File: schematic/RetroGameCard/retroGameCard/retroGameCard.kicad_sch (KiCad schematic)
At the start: 1 part, among them IC1 STM32C562KET6

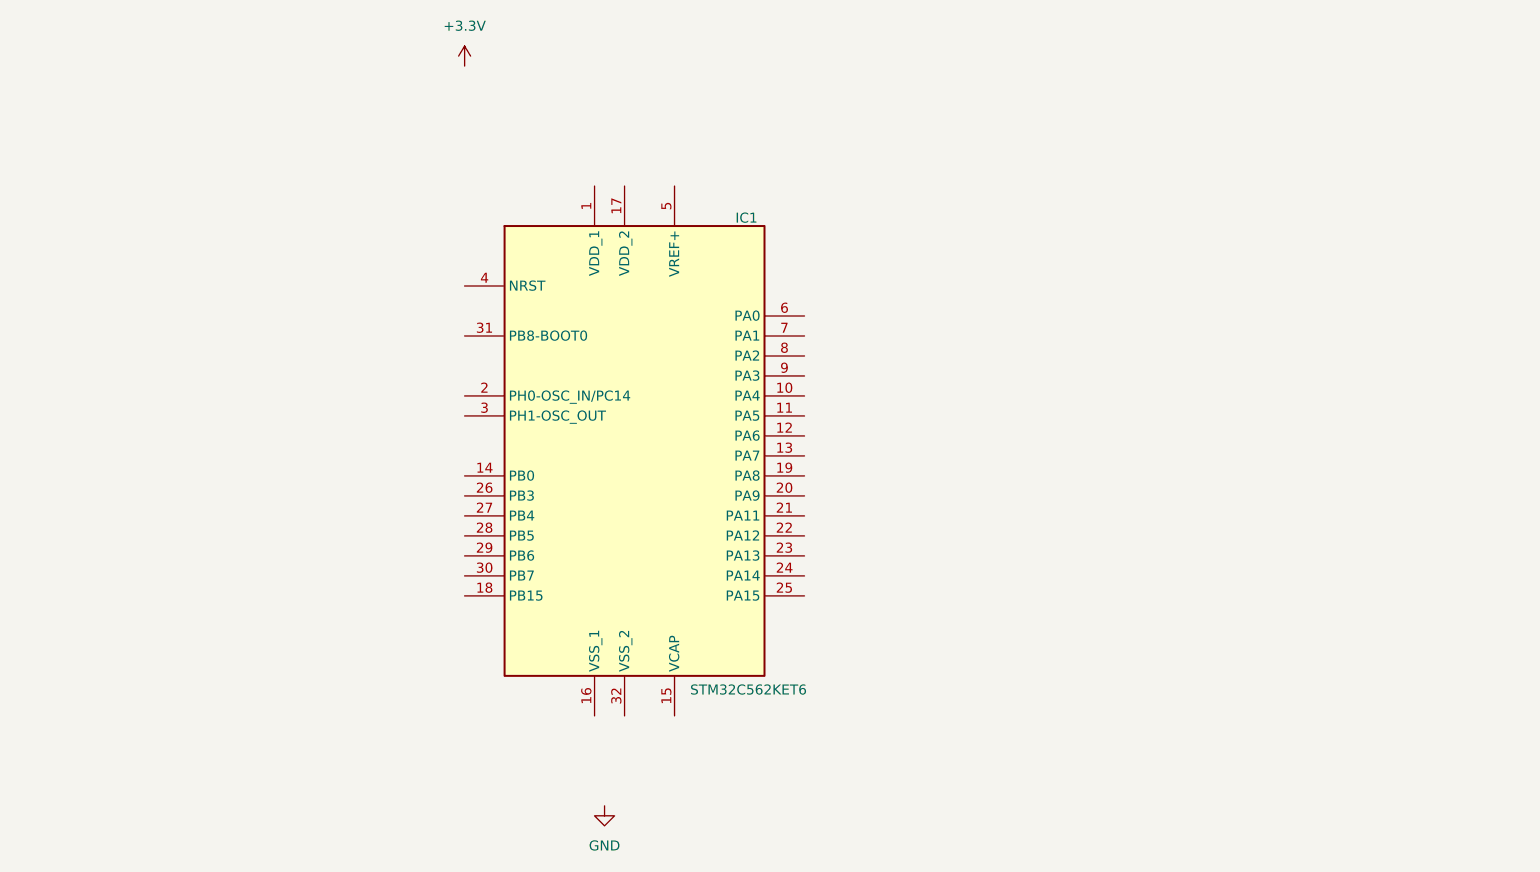
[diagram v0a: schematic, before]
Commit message: added schematic for USB, debug and oled
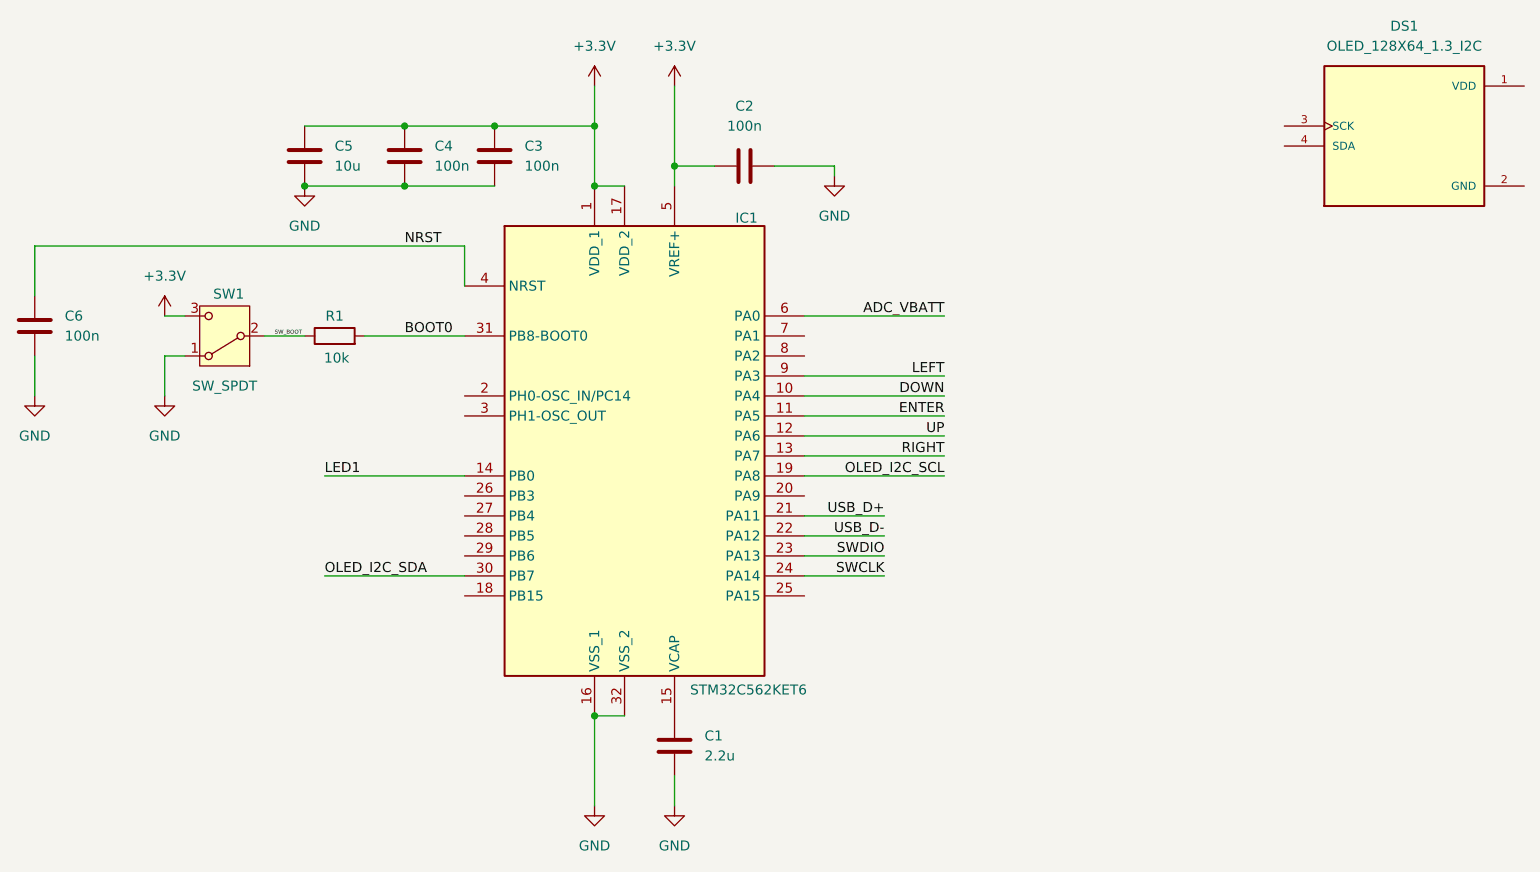
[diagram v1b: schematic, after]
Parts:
- added C1: 2.2u, symbol Device:C
- added C2, C3, C4, C6: 100n, symbol Device:C
- added C5: 10u, symbol Device:C
- added DS1: OLED_128X64_1.3_I2C, OLED_128X64_1.3_I2C:LCD_OLED_128X64_1.3_I2C, symbol OLED_128X64_1.3_I2C:OLED_128X64_1.3_I2C
- added R1: 10k, symbol Device:R
- added SW1: SW_SPDT, symbol Switch:SW_SPDT
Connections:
- net +3.3V: now also IC1.1 (VDD_1), IC1.17 (VDD_2), IC1.5 (VREF+), C2.1, C3.1, C4.1, C5.1, SW1.3 (C)
- net GND: now also IC1.16 (VSS_1), IC1.32 (VSS_2), C1.2, C2.2, C3.2, C4.2, C5.2, C6.2, SW1.1 (A)
- net DOWN: now reaches IC1.10 (PA4)
- net ENTER: now reaches IC1.11 (PA5)
- net UP: now reaches IC1.12 (PA6)
- net RIGHT: now reaches IC1.13 (PA7)
- net LED1: now reaches IC1.14 (PB0)
- net at IC1.15 (VCAP): now also C1.1
- net OLED_I2C_SCL: now reaches IC1.19 (PA8)
- net USB_D+: now reaches IC1.21 (PA11)
- net USB_D-: now reaches IC1.22 (PA12)
- net SWDIO: now reaches IC1.23 (PA13)
- net SWCLK: now reaches IC1.24 (PA14)
- net OLED_I2C_SDA: now reaches IC1.30 (PB7)
- net BOOT0: now reaches IC1.31 (PB8-BOOT0)
- net BOOT0: now also R1.2
- net NRST: now reaches IC1.4 (NRST)
- net NRST: now also C6.1
- net ADC_VBATT: now reaches IC1.6 (PA0)
- net LEFT: now reaches IC1.9 (PA3)
- new net SW_BOOT: R1.1, SW1.2 (B)

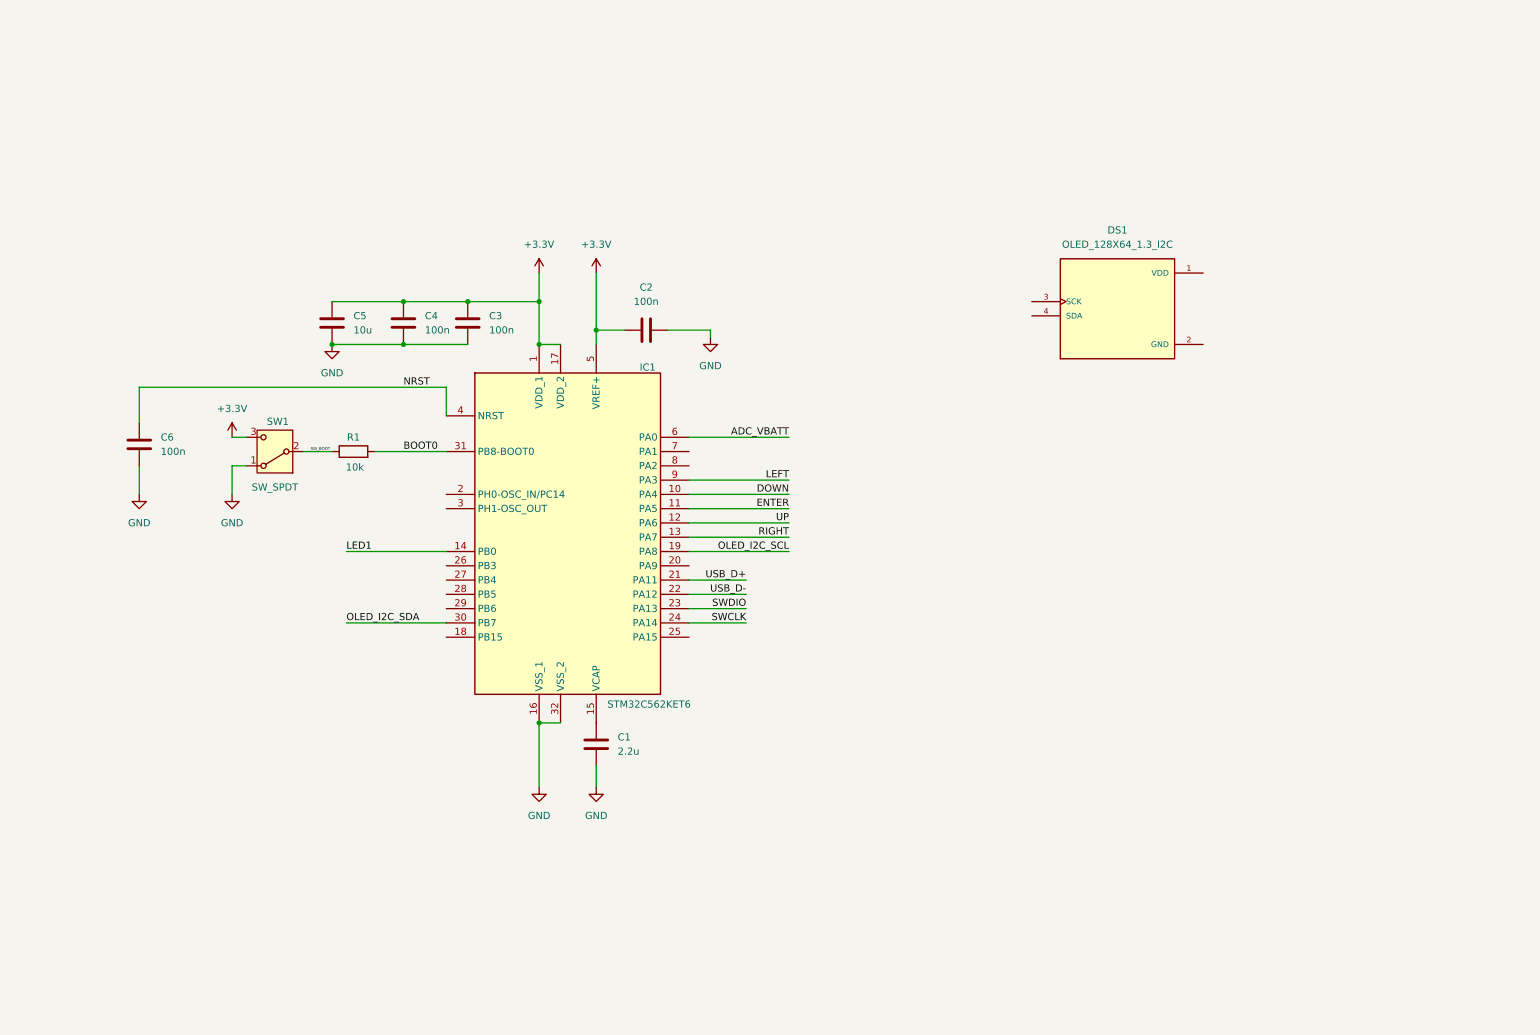
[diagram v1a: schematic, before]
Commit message: added usb circut, to do battery manegement
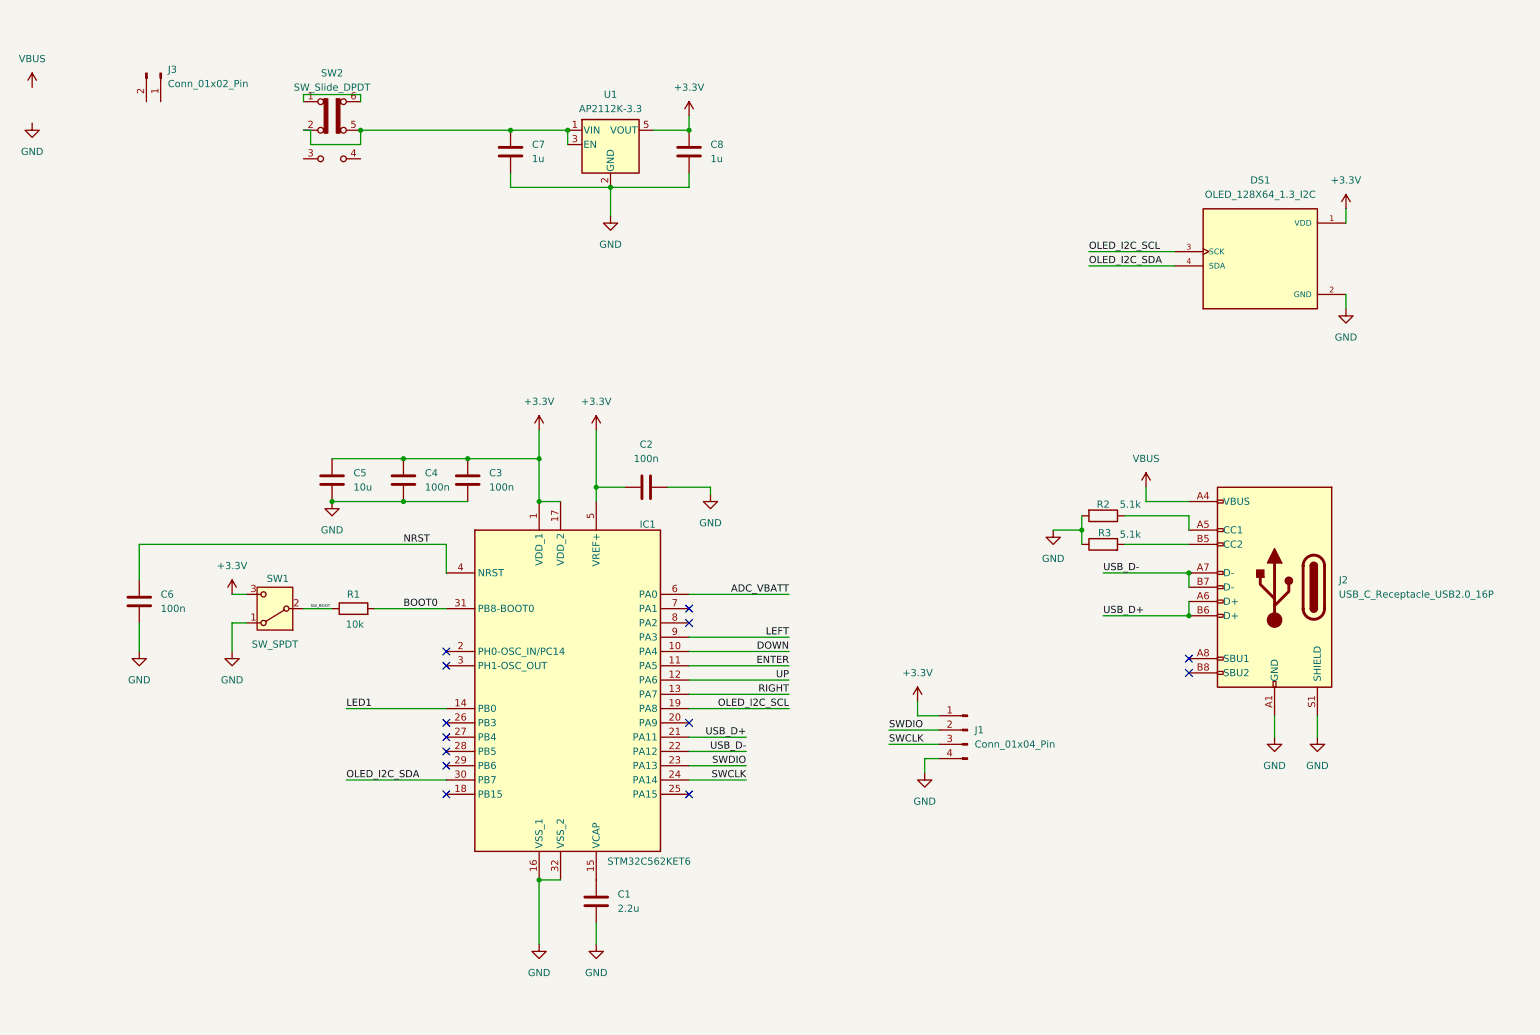
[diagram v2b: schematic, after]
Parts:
- added C7, C8: 1u, symbol Device:C
- added J1: Conn_01x04_Pin, symbol Connector:Conn_01x04_Pin
- added J2: USB_C_Receptacle_USB2.0_16P, symbol Connector:USB_C_Receptacle_USB2.0_16P
- added J3: Conn_01x02_Pin, symbol Connector:Conn_01x02_Pin
- added R2, R3: 5.1k, symbol Device:R
- added SW2: SW_Slide_DPDT, symbol Switch:SW_Slide_DPDT
- added U1: AP2112K-3.3, Package_TO_SOT_SMD:SOT-23-5, symbol Regulator_Linear:AP2112K-3.3
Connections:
- net +3.3V: now also DS1.1 (VDD), C8.1, J1.1 (Pin_1), U1.5 (VOUT)
- net GND: now also DS1.2 (GND), C7.2, C8.2, J1.4 (Pin_4), J2.A1 (GND), J2.A12 (GND), J2.B1 (GND), J2.B12 (GND), J2.S1 (SHIELD), R2.2, R3.1, U1.2 (GND)
- net OLED_I2C_SCL: now also DS1.3 (SCK)
- net OLED_I2C_SDA: now also DS1.4 (SDA)
- net SWCLK: now also J1.3 (Pin_3)
- net SWDIO: now also J1.2 (Pin_2)
- net USB_D+: now also J2.A6 (D+), J2.B6 (D+)
- net USB_D-: now also J2.A7 (D-), J2.B7 (D-)
- new net: C7.1, SW2.2 (B), SW2.5 (B), U1.1 (VIN), U1.3 (EN)
- new net: J2.B5 (CC2), R3.2
- new net: SW2.1 (A), SW2.6 (C)
- new net: J2.A5 (CC1), R2.1
- new net VBUS: J2.A4 (VBUS), J2.A9 (VBUS), J2.B4 (VBUS), J2.B9 (VBUS)
- no-connect marks 0 -> 13
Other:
- moved on the sheet: C1, C2, C3, C4, C5, C6, DS1, IC1, R1, SW1

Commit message: added charging 1s lipo
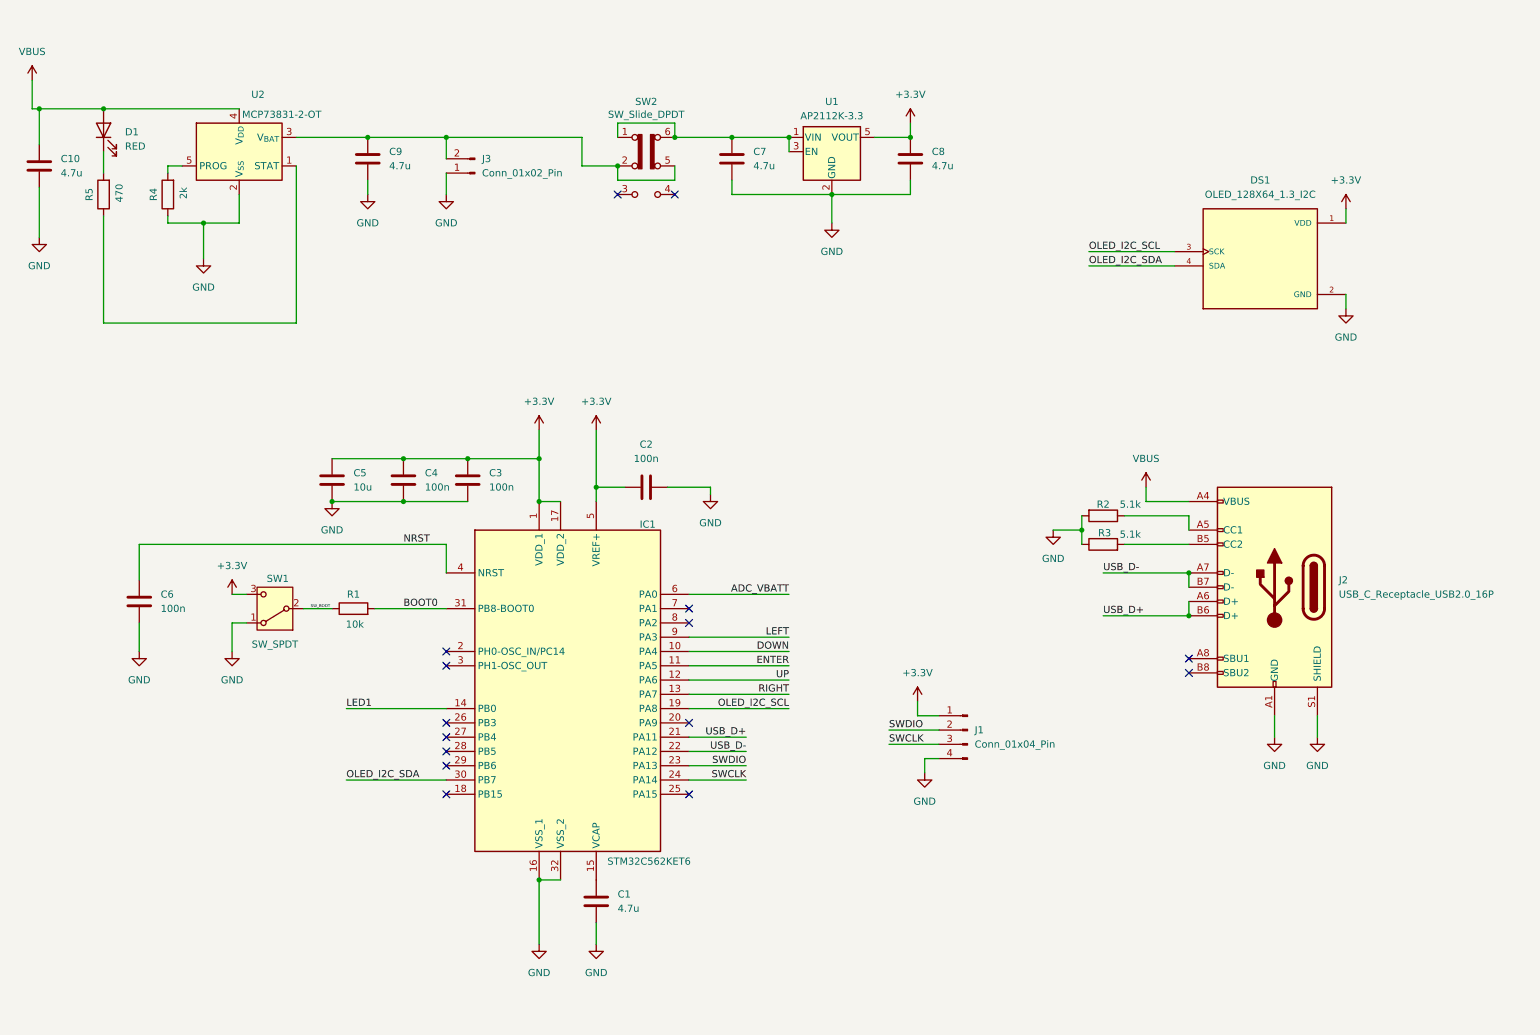
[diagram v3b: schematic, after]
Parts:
- added C10, C9: 4.7u, symbol Device:C
- added D1: RED, symbol Device:LED
- added R4: 2k, symbol Device:R
- added R5: 470, symbol Device:R
- added U2: MCP73831-2-OT, Package_TO_SOT_SMD:SOT-23-5, symbol Battery_Management:MCP73831-2-OT
- C1: value 2.2u -> 4.7u
- C7, C8: value 1u -> 4.7u
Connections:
- net GND: now also J3.1 (Pin_1), C10.2, C9.2, R4.1, U2.2 (V_{SS})
- net VBUS: now also C10.1, D1.2 (A), U2.4 (V_{DD})
- net at J3.2 (Pin_2): now also SW2.2 (B), SW2.5 (B), C9.1, U2.3 (V_{BAT})
- net at C7.1, U1.1 (VIN), U1.3 (EN): now also SW2.1 (A), SW2.6 (C); no longer SW2.2 (B), SW2.5 (B)
- new net: D1.1 (K), R5.2
- new net: R5.1, U2.1 (STAT)
- new net: R4.2, U2.5 (PROG)
- no-connect marks 13 -> 15
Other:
- moved on the sheet: C7, C8, J3, SW2, U1

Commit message: final schematic
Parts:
- removed DS1: OLED_128X64_1.3_I2C, OLED_128X64_1.3_I2C:LCD_OLED_128X64_1.3_I2C, symbol OLED_128X64_1.3_I2C:OLED_128X64_1.3_I2C
- removed J3: Conn_01x02_Pin, symbol Connector:Conn_01x02_Pin
- added C11: 1s lipo battery, symbol Device:C
- added D2: RED, symbol Device:LED
- added J1: Conn_01x04_Pin, symbol Connector:Conn_01x04_Pin
- added R6: 2k, symbol Device:R
- added R7, R8: 100k, symbol Device:R
- added SW3, SW4, SW5, SW6, SW7: SW_Push, symbol Switch:SW_Push
- renumbered C10 to C1, C1 to C10, C9 to C2, C7 to C3, C8 to C4, C4 to C6, C3 to C7, C2 to C8, C6 to C9, J1 to J2, J2 to J3, R5 to R1, R4 to R2, R2 to R3, R3 to R4, R1 to R5, SW2 to SW1, SW1 to SW2, U2 to U1, U1 to U2
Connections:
- net +3.3V: now also J1.1 (Pin_1)
- net ADC_VBATT: now also R7.1, R8.2
- net DOWN: now also SW4.1
- net ENTER: now also SW5.1
- net GND: now also C11.2, J1.4 (Pin_4), R6.1, R8.1, SW3.2, SW4.2, SW5.2, SW6.2, SW7.2
- net LEFT: now also SW3.1
- net OLED_I2C_SCL: now also J1.2 (Pin_2)
- net OLED_I2C_SDA: now also J1.3 (Pin_3)
- net RIGHT: now also SW7.1
- net UP: now also SW6.1
- net USB_D+: now also IC1.22 (PA12); no longer IC1.21 (PA11)
- net USB_D-: now also IC1.21 (PA11); no longer IC1.22 (PA12)
- net Vbat: now reaches C2.1, SW1.2 (B), SW1.5 (B), U1.3 (V_{BAT})
- net Vbat: now also C11.1, R7.2
- net LED1: no longer names the net of IC1.14 (PB0)
- net LED1: now also D2.2 (A)
- new net: D2.1 (K), R6.2
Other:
- note added: "1x 100nF per VDD pin"
- note added: "ADC_Vbat"
- note added: "BUTTONS"
- note added: "DEBUG"
- note added: "MICROCONTROLER"
- note added: "PCB GAME CARD"
- note added: "POWER SUPPLY"
- note added: "Pinout using STM32MX2"
- note added: "SSD1306"
- note added: "USB"
- note added: "VBUS from USB connector (nom. +5V) Min.1uF inp./outp. caps C11 - 1s lipo battery"
- note added: "datasheet MCP73831/2 page 1"
- title: (none) -> PCB GAME CARD V1
- moved on the sheet: C1, C10, C2, C3, C4, C5, C6, C7, C8, C9, D1, IC1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
